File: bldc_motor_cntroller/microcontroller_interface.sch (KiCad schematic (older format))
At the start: 15 parts

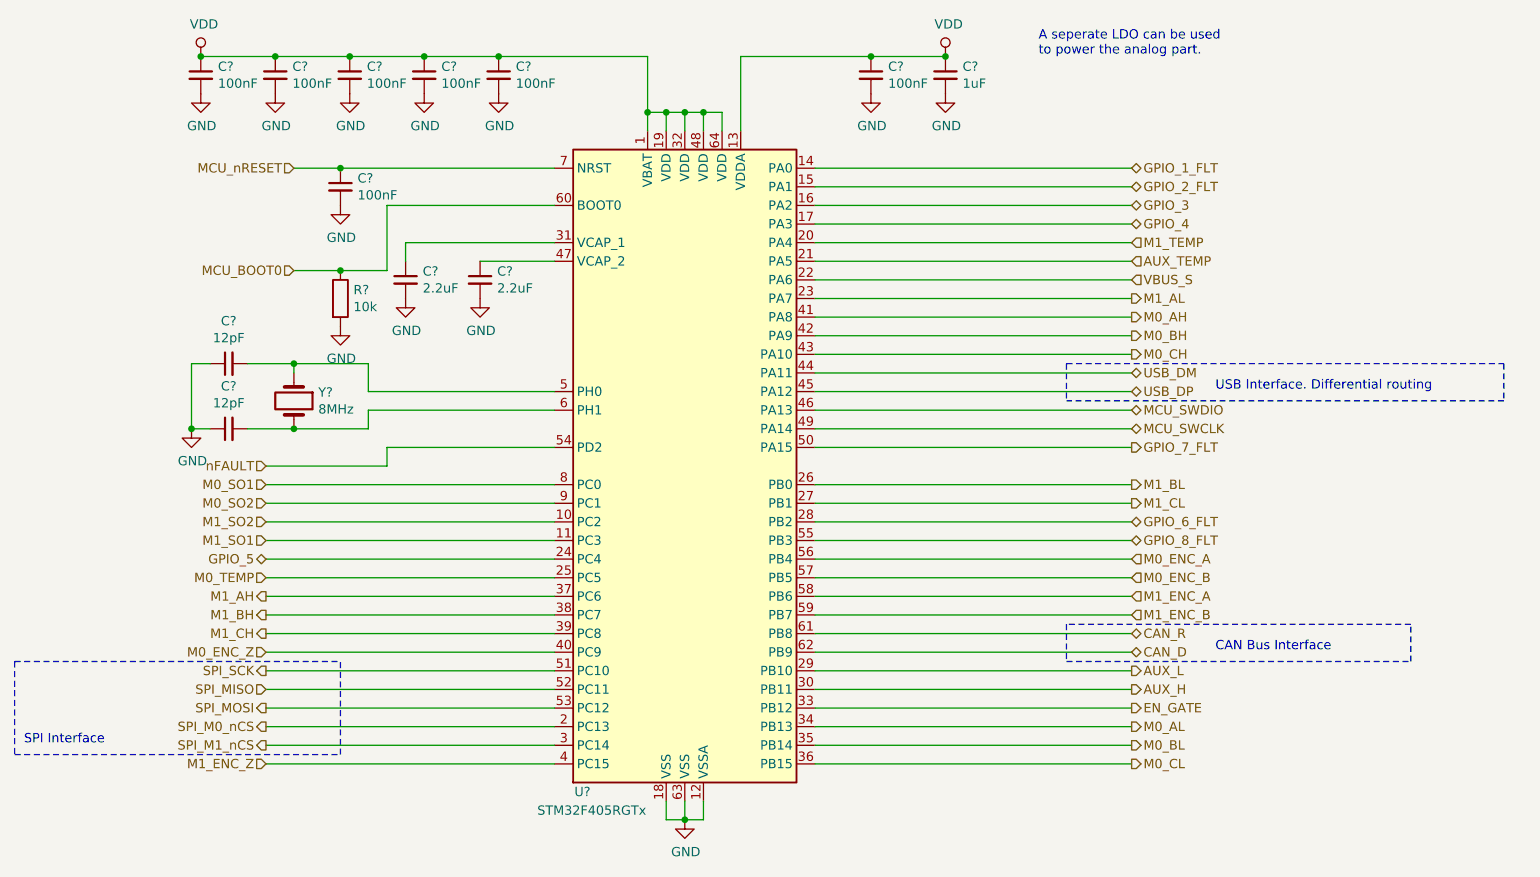
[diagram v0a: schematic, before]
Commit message: schematic annotation. added bulk caps. moved shunt res to powersheet.
Signed-off-by: azmat bilal <azmat.bilal@outlook.com>
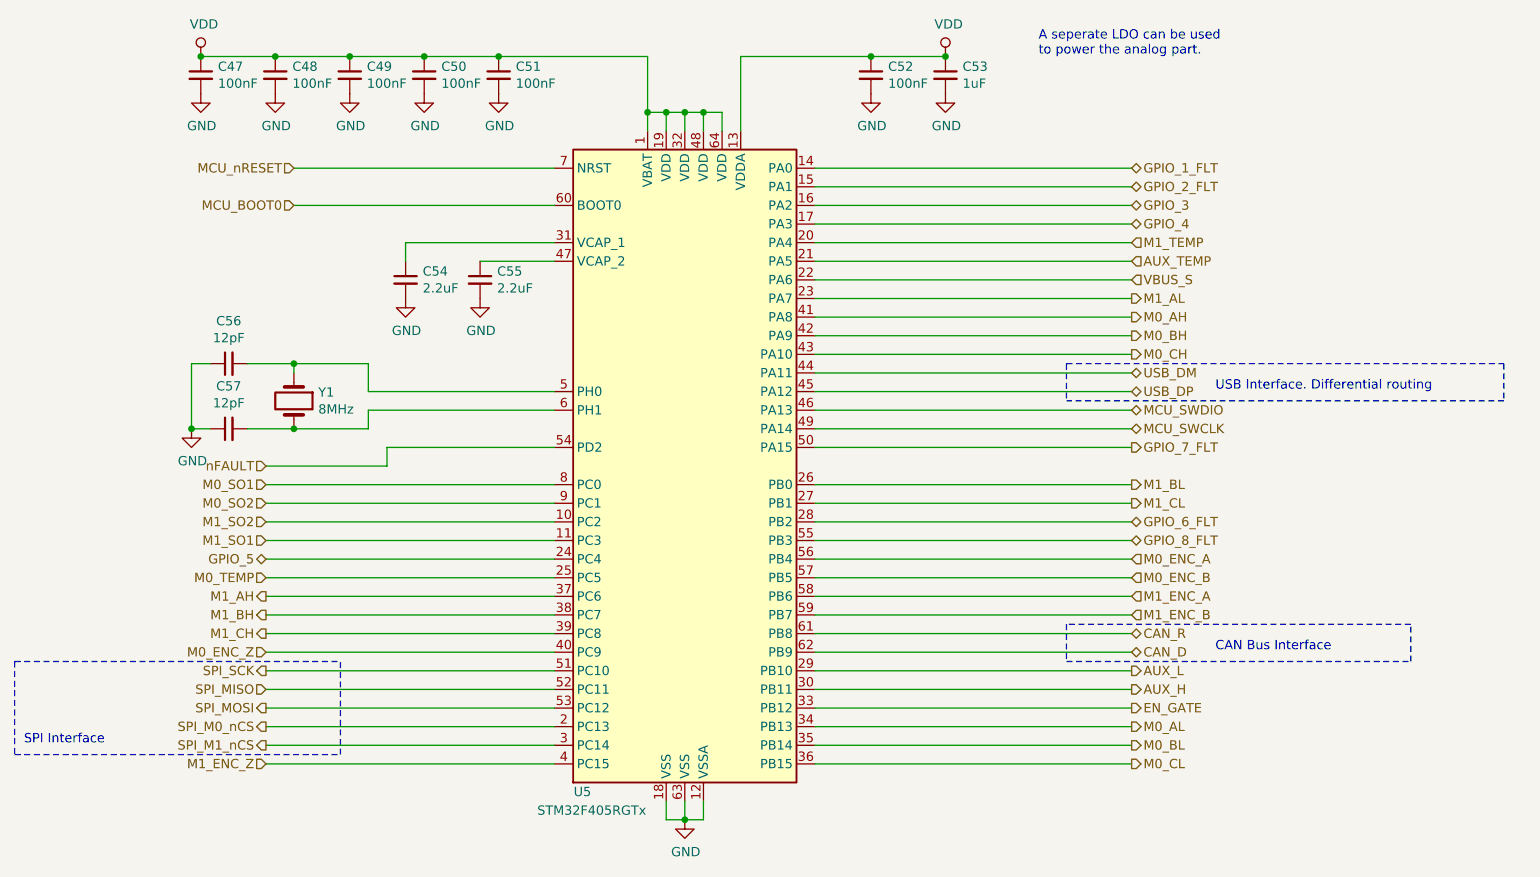
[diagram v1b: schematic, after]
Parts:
- removed C?: 100nF, Capacitor_SMD:C_0402_1005Metric, symbol Device:C_Small
- removed R?: 10k, Resistor_SMD:R_0402_1005Metric, symbol Device:R
- gave numbers to parts that had none: 13
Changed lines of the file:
@@
 $Descr A4 11693 8268
 encoding utf-8
-Sheet 2 6
+Sheet 5 5
 Title ""
 Date ""
@@
 $EndDescr
 $Comp
-L MCU_ST_STM32F4:STM32F405RGTx U?
+L MCU_ST_STM32F4:STM32F405RGTx U5
 U 1 1 5E2D979D
 P 5600 3700
-F 0 "U?" H 5050 1950 50  0000 C CNN
+F 0 "U5" H 5050 1950 50  0000 C CNN
 F 1 "STM32F405RGTx" H 5100 1850 50  0000 C CNN
 F 2 "Package_QFP:LQFP-64_10x10mm_P0.5mm" H 5000 2000 50  0001 R CNN
@@
 	5700 5600 5600 5600
 $Comp
-L Device:C_Small C?
+L Device:C_Small C47
 U 1 1 5E2E2854
 P 3000 1600
-F 0 "C?" H 3092 1646 50  0000 L CNN
+F 0 "C47" H 3092 1646 50  0000 L CNN
 F 1 "100nF" H 3092 1555 50  0000 L CNN
 F 2 "" H 3000 1600 50  0001 C CNN
@@
 $EndComp
 $Comp
-L Device:C_Small C?
+L Device:C_Small C48
 U 1 1 5E2E2E09
 P 3400 1600
-F 0 "C?" H 3492 1646 50  0000 L CNN
+F 0 "C48" H 3492 1646 50  0000 L CNN
 F 1 "100nF" H 3492 1555 50  0000 L CNN
 F 2 "" H 3400 1600 50  0001 C CNN
@@
 $EndComp
 $Comp
-L Device:C_Small C?
+L Device:C_Small C49
 U 1 1 5E2E3167
 P 3800 1600
-F 0 "C?" H 3892 1646 50  0000 L CNN
+F 0 "C49" H 3892 1646 50  0000 L CNN
 F 1 "100nF" H 3892 1555 50  0000 L CNN
 F 2 "Capacitor_SMD:C_0402_1005Metric" H 3800 1600 50  0001 C CNN
@@
 $EndComp
 $Comp
-L Device:C_Small C?
+L Device:C_Small C50
 U 1 1 5E2E33CD
 P 4200 1600
-F 0 "C?" H 4292 1646 50  0000 L CNN
+F 0 "C50" H 4292 1646 50  0000 L CNN
 F 1 "100nF" H 4292 1555 50  0000 L CNN
 F 2 "" H 4200 1600 50  0001 C CNN
@@
 $EndComp
 $Comp
-L Device:C_Small C?
+L Device:C_Small C51
 U 1 1 5E2E3617
 P 4600 1600
-F 0 "C?" H 4692 1646 50  0000 L CNN
+F 0 "C51" H 4692 1646 50  0000 L CNN
 F 1 "100nF" H 4692 1555 50  0000 L CNN
 F 2 "" H 4600 1600 50  0001 C CNN
@@
 $EndComp
 $Comp
-L Device:C_Small C?
+L Device:C_Small C53
 U 1 1 5E2E66D1
 P 7000 1600
-F 0 "C?" H 7092 1646 50  0000 L CNN
+F 0 "C53" H 7092 1646 50  0000 L CNN
 F 1 "1uF" H 7092 1555 50  0000 L CNN
 F 2 "" H 7000 1600 50  0001 C CNN
@@
 $EndComp
 $Comp
-L Device:C_Small C?
+L Device:C_Small C52
 U 1 1 5E2E6F13
 P 6600 1600
-F 0 "C?" H 6692 1646 50  0000 L CNN
+F 0 "C52" H 6692 1646 50  0000 L CNN
 F 1 "100nF" H 6692 1555 50  0000 L CNN
 F 2 "" H 6600 1600 50  0001 C CNN
@@
 	1    0    0    -1
 $EndComp
-Wire Wire Line
-	3500 2100 3750 2100
-$Comp
-L Device:C_Small C?
-U 1 1 5E2EC166
-P 3750 2200
-F 0 "C?" H 3842 2246 50  0000 L CNN
-F 1 "100nF" H 3842 2155 50  0000 L CNN
-F 2 "Capacitor_SMD:C_0402_1005Metric" H 3750 2200 50  0001 C CNN
-F 3 "~" H 3750 2200 50  0001 C CNN
-	1    3750 2200
-	1    0    0    -1
-$EndComp
-Connection ~ 3750 2100
-Wire Wire Line
-	3750 2100 4900 2100
 Text HLabel 3500 2100 0    50   Input ~ 0
 MCU_nRESET
 $Comp
-L Device:C_Small C?
+L Device:C_Small C55
 U 1 1 5E2ED258
 P 4500 2700
-F 0 "C?" H 4592 2746 50  0000 L CNN
+F 0 "C55" H 4592 2746 50  0000 L CNN
 F 1 "2.2uF" H 4592 2655 50  0000 L CNN
 F 2 "Capacitor_SMD:C_0402_1005Metric" H 4500 2700 50  0001 C CNN
@@
 $EndComp
 $Comp
-L Device:C_Small C?
+L Device:C_Small C54
 U 1 1 5E2EDC07
 P 4100 2700
-F 0 "C?" H 4192 2746 50  0000 L CNN
+F 0 "C54" H 4192 2746 50  0000 L CNN
 F 1 "2.2uF" H 4192 2655 50  0000 L CNN
 F 2 "Capacitor_SMD:C_0402_1005Metric" H 4100 2700 50  0001 C CNN
@@
 	4500 2600 4900 2600
 $Comp
-L Device:Crystal Y?
+L Device:Crystal Y1
 U 1 1 5E2EF4F2
 P 3500 3350
-F 0 "Y?" V 3454 3481 50  0000 L CNN
+F 0 "Y1" V 3454 3481 50  0000 L CNN
 F 1 "8MHz" V 3545 3481 50  0000 L CNN
 F 2 "Crystal:Crystal_SMD_Abracon_ABM3-2Pin_5.0x3.2mm" H 3500 3350 50  0001 C CNN
@@
 $EndComp
 $Comp
-L Device:C_Small C?
+L Device:C_Small C57
 U 1 1 5E2F1862
 P 3150 3500
-F 0 "C?" V 3379 3500 50  0000 C CNN
+F 0 "C57" V 3379 3500 50  0000 C CNN
 F 1 "12pF" V 3288 3500 50  0000 C CNN
 F 2 "Capacitor_SMD:C_0402_1005Metric" H 3150 3500 50  0001 C CNN
@@
 $EndComp
 $Comp
-L Device:C_Small C?
+L Device:C_Small C56
 U 1 1 5E2F208E
 P 3150 3150
-F 0 "C?" V 3379 3150 50  0000 C CNN
+F 0 "C56" V 3379 3150 50  0000 C CNN
 F 1 "12pF" V 3288 3150 50  0000 C CNN
 F 2 "Capacitor_SMD:C_0402_1005Metric" H 3150 3150 50  0001 C CNN
@@
 	3050 3500 2950 3500
 Connection ~ 2950 3500
-Text HLabel 3500 2650 0    50   Input ~ 0
+Text HLabel 3500 2300 0    50   Input ~ 0
 MCU_BOOT0
-Wire Wire Line
-	4000 2650 4000 2300
-Wire Wire Line
-	4000 2300 4900 2300
-Wire Wire Line
-	3500 2650 3750 2650
-$Comp
-L Device:R R?
-U 1 1 5E2FBF77
-P 3750 2800
-F 0 "R?" H 3820 2846 50  0000 L CNN
-F 1 "10k" H 3820 2755 50  0000 L CNN
-F 2 "Resistor_SMD:R_0402_1005Metric" V 3680 2800 50  0001 C CNN
-F 3 "~" H 3750 2800 50  0001 C CNN
-	1    3750 2800
-	1    0    0    -1
-$EndComp
-Connection ~ 3750 2650
-Wire Wire Line
-	3750 2650 4000 2650
 Text HLabel 3350 3800 0    50   Input ~ 0
 M0_SO1
@@
 Wire Wire Line
 	6300 2200 8000 2200
-$Comp
-L power:GND #PWR0112
-U 1 1 5E2ECE80
-P 3750 2300
-F 0 "#PWR0112" H 3750 2050 50  0001 C CNN
-F 1 "GND" H 3755 2127 50  0000 C CNN
-F 2 "" H 3750 2300 50  0001 C CNN
-F 3 "" H 3750 2300 50  0001 C CNN
-	1    3750 2300
-	1    0    0    -1
-$EndComp
-$Comp
-L power:GND #PWR0113
-U 1 1 5E2FC3D3
-P 3750 2950
-F 0 "#PWR0113" H 3750 2700 50  0001 C CNN
-F 1 "GND" H 3755 2777 50  0000 C CNN
-F 2 "" H 3750 2950 50  0001 C CNN
-F 3 "" H 3750 2950 50  0001 C CNN
-	1    3750 2950
-	1    0    0    -1
-$EndComp
 $Comp
 L power:GND #PWR0114
@@
 	3350 5300 4900 5300
 $Comp
-L power:VDD #PWR?
+L power:VDD #PWR0186
 U 1 1 5E3C1303
 P 3000 1500
-F 0 "#PWR?" H 3000 1350 50  0001 C CNN
+F 0 "#PWR0186" H 3000 1350 50  0001 C CNN
 F 1 "VDD" H 3017 1673 50  0000 C CNN
 F 2 "" H 3000 1500 50  0001 C CNN
@@
 Connection ~ 3000 1500
 $Comp
-L power:VDD #PWR?
+L power:VDD #PWR0187
 U 1 1 5E3C1A5D
 P 7000 1500
-F 0 "#PWR?" H 7000 1350 50  0001 C CNN
+F 0 "#PWR0187" H 7000 1350 50  0001 C CNN
 F 1 "VDD" H 7017 1673 50  0000 C CNN
 F 2 "" H 7000 1500 50  0001 C CNN
@@
 $EndComp
 Connection ~ 7000 1500
+Wire Wire Line
+	3500 2100 4900 2100
+Wire Wire Line
+	3500 2300 4900 2300
 $EndSCHEMATC

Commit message: added missing footprints.
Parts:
- C47, C48, C50, C51, C52, C53: footprint (none) -> Capacitor_SMD:C_0402_1005Metric
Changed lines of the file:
@@
 F 0 "C47" H 3092 1646 50  0000 L CNN
 F 1 "100nF" H 3092 1555 50  0000 L CNN
-F 2 "" H 3000 1600 50  0001 C CNN
+F 2 "Capacitor_SMD:C_0402_1005Metric" H 3000 1600 50  0001 C CNN
 F 3 "~" H 3000 1600 50  0001 C CNN
 	1    3000 1600
@@
 F 0 "C48" H 3492 1646 50  0000 L CNN
 F 1 "100nF" H 3492 1555 50  0000 L CNN
-F 2 "" H 3400 1600 50  0001 C CNN
+F 2 "Capacitor_SMD:C_0402_1005Metric" H 3400 1600 50  0001 C CNN
 F 3 "~" H 3400 1600 50  0001 C CNN
 	1    3400 1600
@@
 F 0 "C50" H 4292 1646 50  0000 L CNN
 F 1 "100nF" H 4292 1555 50  0000 L CNN
-F 2 "" H 4200 1600 50  0001 C CNN
+F 2 "Capacitor_SMD:C_0402_1005Metric" H 4200 1600 50  0001 C CNN
 F 3 "~" H 4200 1600 50  0001 C CNN
 	1    4200 1600
@@
 F 0 "C51" H 4692 1646 50  0000 L CNN
 F 1 "100nF" H 4692 1555 50  0000 L CNN
-F 2 "" H 4600 1600 50  0001 C CNN
+F 2 "Capacitor_SMD:C_0402_1005Metric" H 4600 1600 50  0001 C CNN
 F 3 "~" H 4600 1600 50  0001 C CNN
 	1    4600 1600
@@
 F 0 "C53" H 7092 1646 50  0000 L CNN
 F 1 "1uF" H 7092 1555 50  0000 L CNN
-F 2 "" H 7000 1600 50  0001 C CNN
+F 2 "Capacitor_SMD:C_0402_1005Metric" H 7000 1600 50  0001 C CNN
 F 3 "~" H 7000 1600 50  0001 C CNN
 	1    7000 1600
@@
 F 0 "C52" H 6692 1646 50  0000 L CNN
 F 1 "100nF" H 6692 1555 50  0000 L CNN
-F 2 "" H 6600 1600 50  0001 C CNN
+F 2 "Capacitor_SMD:C_0402_1005Metric" H 6600 1600 50  0001 C CNN
 F 3 "~" H 6600 1600 50  0001 C CNN
 	1    6600 1600

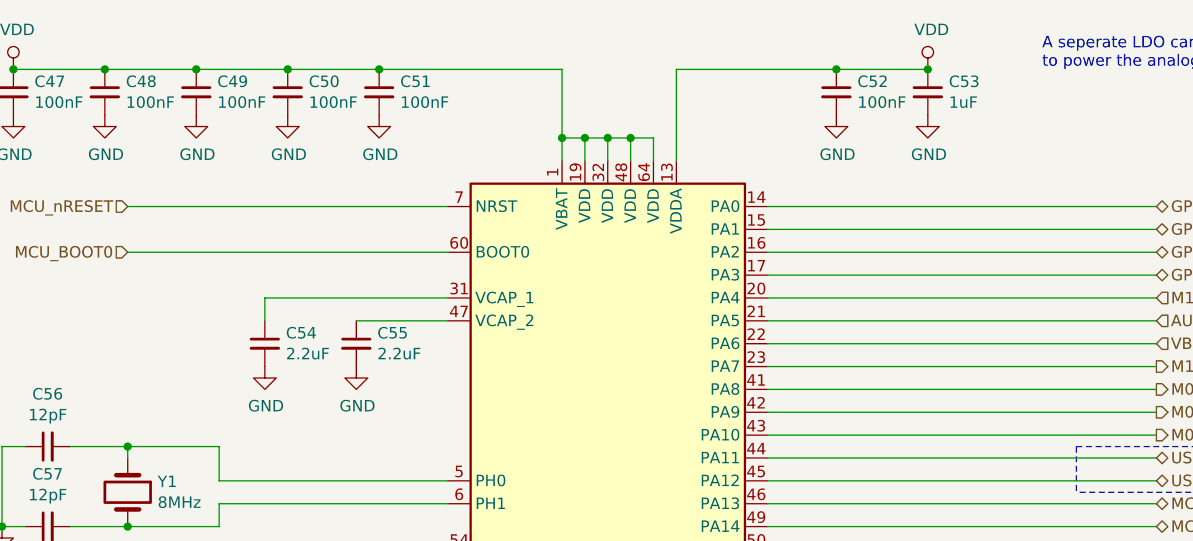
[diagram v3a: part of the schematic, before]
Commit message: improved BOM
Signed-off-by: azmat bilal <azmat.bilal@outlook.com>
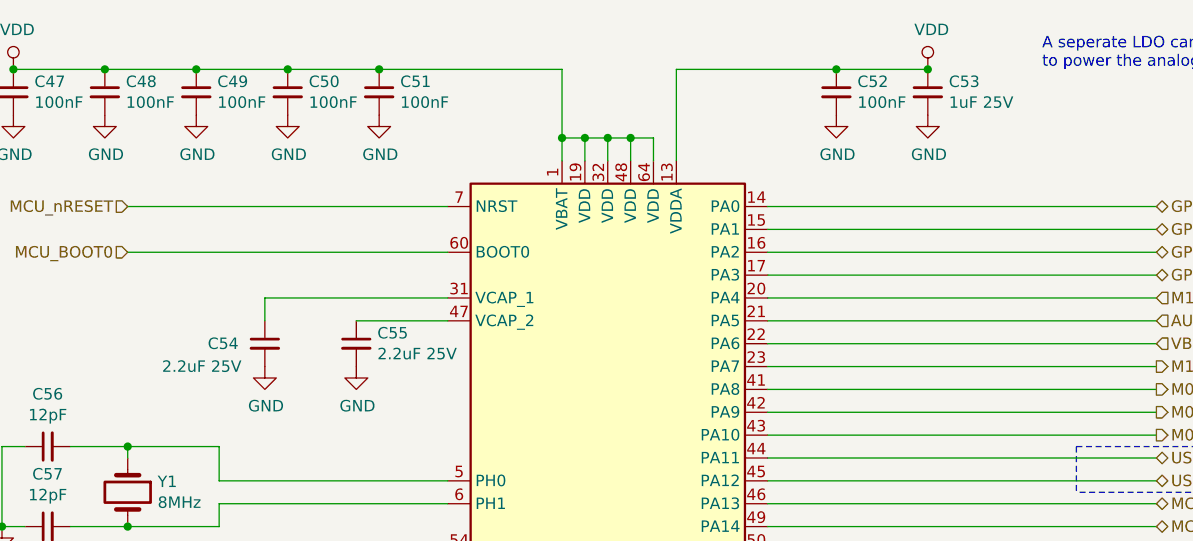
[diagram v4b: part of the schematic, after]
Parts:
- C47, C48, C49, C50, C51, C52: MPN (none) -> GRM155R62A104KE14D
- C53: value 1uF -> 1uF 25V; MPN (none) -> GMK105CC6105MV-F
- C54, C55: value 2.2uF -> 2.2uF 25V; MPN (none) -> GRM155C81E225KE11D
- C56, C57: MPN (none) -> GCQ1555C1H120FB01D
- U5: MPN (none) -> STM32F405RGT7
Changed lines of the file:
@@
 F 2 "Package_QFP:LQFP-64_10x10mm_P0.5mm" H 5000 2000 50  0001 R CNN
 F 3 "http://www.st.com/st-web-ui/static/active/en/resource/technical/document/datasheet/DM00037051.pdf" H 5600 3700 50  0001 C CNN
+F 4 "STM32F405RGT7" H 5600 3700 50  0001 C CNN "MPN"
 	1    5600 3700
 	1    0    0    -1
@@
 F 2 "Capacitor_SMD:C_0402_1005Metric" H 3000 1600 50  0001 C CNN
 F 3 "~" H 3000 1600 50  0001 C CNN
+F 4 "GRM155R62A104KE14D" H 3000 1600 50  0001 C CNN "MPN"
 	1    3000 1600
 	1    0    0    -1
@@
 F 2 "Capacitor_SMD:C_0402_1005Metric" H 3400 1600 50  0001 C CNN
 F 3 "~" H 3400 1600 50  0001 C CNN
+F 4 "GRM155R62A104KE14D" H 3400 1600 50  0001 C CNN "MPN"
 	1    3400 1600
 	1    0    0    -1
@@
 F 2 "Capacitor_SMD:C_0402_1005Metric" H 3800 1600 50  0001 C CNN
 F 3 "~" H 3800 1600 50  0001 C CNN
+F 4 "GRM155R62A104KE14D" H 3800 1600 50  0001 C CNN "MPN"
 	1    3800 1600
 	1    0    0    -1
@@
 F 2 "Capacitor_SMD:C_0402_1005Metric" H 4200 1600 50  0001 C CNN
 F 3 "~" H 4200 1600 50  0001 C CNN
+F 4 "GRM155R62A104KE14D" H 4200 1600 50  0001 C CNN "MPN"
 	1    4200 1600
 	1    0    0    -1
@@
 F 2 "Capacitor_SMD:C_0402_1005Metric" H 4600 1600 50  0001 C CNN
 F 3 "~" H 4600 1600 50  0001 C CNN
+F 4 "GRM155R62A104KE14D" H 4600 1600 50  0001 C CNN "MPN"
 	1    4600 1600
 	1    0    0    -1
@@
 P 7000 1600
 F 0 "C53" H 7092 1646 50  0000 L CNN
-F 1 "1uF" H 7092 1555 50  0000 L CNN
+F 1 "1uF 25V" H 7092 1555 50  0000 L CNN
 F 2 "Capacitor_SMD:C_0402_1005Metric" H 7000 1600 50  0001 C CNN
 F 3 "~" H 7000 1600 50  0001 C CNN
+F 4 "GMK105CC6105MV-F" H 7000 1600 50  0001 C CNN "MPN"
 	1    7000 1600
 	1    0    0    -1
@@
 F 2 "Capacitor_SMD:C_0402_1005Metric" H 6600 1600 50  0001 C CNN
 F 3 "~" H 6600 1600 50  0001 C CNN
+F 4 "GRM155R62A104KE14D" H 6600 1600 50  0001 C CNN "MPN"
 	1    6600 1600
 	1    0    0    -1
@@
 P 4500 2700
 F 0 "C55" H 4592 2746 50  0000 L CNN
-F 1 "2.2uF" H 4592 2655 50  0000 L CNN
+F 1 "2.2uF 25V" H 4592 2655 50  0000 L CNN
 F 2 "Capacitor_SMD:C_0402_1005Metric" H 4500 2700 50  0001 C CNN
 F 3 "~" H 4500 2700 50  0001 C CNN
+F 4 "GRM155C81E225KE11D" H 4500 2700 50  0001 C CNN "MPN"
 	1    4500 2700
 	1    0    0    -1
@@
 U 1 1 5E2EDC07
 P 4100 2700
-F 0 "C54" H 4192 2746 50  0000 L CNN
-F 1 "2.2uF" H 4192 2655 50  0000 L CNN
+F 0 "C54" H 3850 2700 50  0000 L CNN
+F 1 "2.2uF 25V" H 3650 2600 50  0000 L CNN
 F 2 "Capacitor_SMD:C_0402_1005Metric" H 4100 2700 50  0001 C CNN
 F 3 "~" H 4100 2700 50  0001 C CNN
+F 4 "GRM155C81E225KE11D" H 4100 2700 50  0001 C CNN "MPN"
 	1    4100 2700
 	1    0    0    -1
@@
 F 2 "Capacitor_SMD:C_0402_1005Metric" H 3150 3500 50  0001 C CNN
 F 3 "~" H 3150 3500 50  0001 C CNN
+F 4 "GCQ1555C1H120FB01D" H 3150 3500 50  0001 C CNN "MPN"
 	1    3150 3500
 	0    -1   -1   0
@@
 F 2 "Capacitor_SMD:C_0402_1005Metric" H 3150 3150 50  0001 C CNN
 F 3 "~" H 3150 3150 50  0001 C CNN
+F 4 "GCQ1555C1H120FB01D" H 3150 3150 50  0001 C CNN "MPN"
 	1    3150 3150
 	0    -1   -1   0
